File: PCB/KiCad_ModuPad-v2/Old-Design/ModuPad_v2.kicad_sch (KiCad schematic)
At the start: 95 parts, among them J1 Conn_01x02, J2 OLED_128x32, SW1 SW_Push, SW10 SW_Push, SW11 SW_Push, SW12 SW_Push, SW13 SW_Push, SW14 SW_Push, SW15 SW_Push, SW16 SW_Push, SW17 SW_Push, SW18 SW_Push, SW19 SW_Push, SW2 SW_Push, SW20 SW_Push, SW21 SW_Push, SW22 SW_Push, SW23 SW_Push, SW24 SW_Push, SW25 SW_Push, SW27_RST1 SW_Push_45deg, SW3 SW_Push, SW4 SW_Push, SW5 SW_Push, SW6 SW_Push, SW7 SW_Push, SW8 SW_Push, SW9 SW_Push

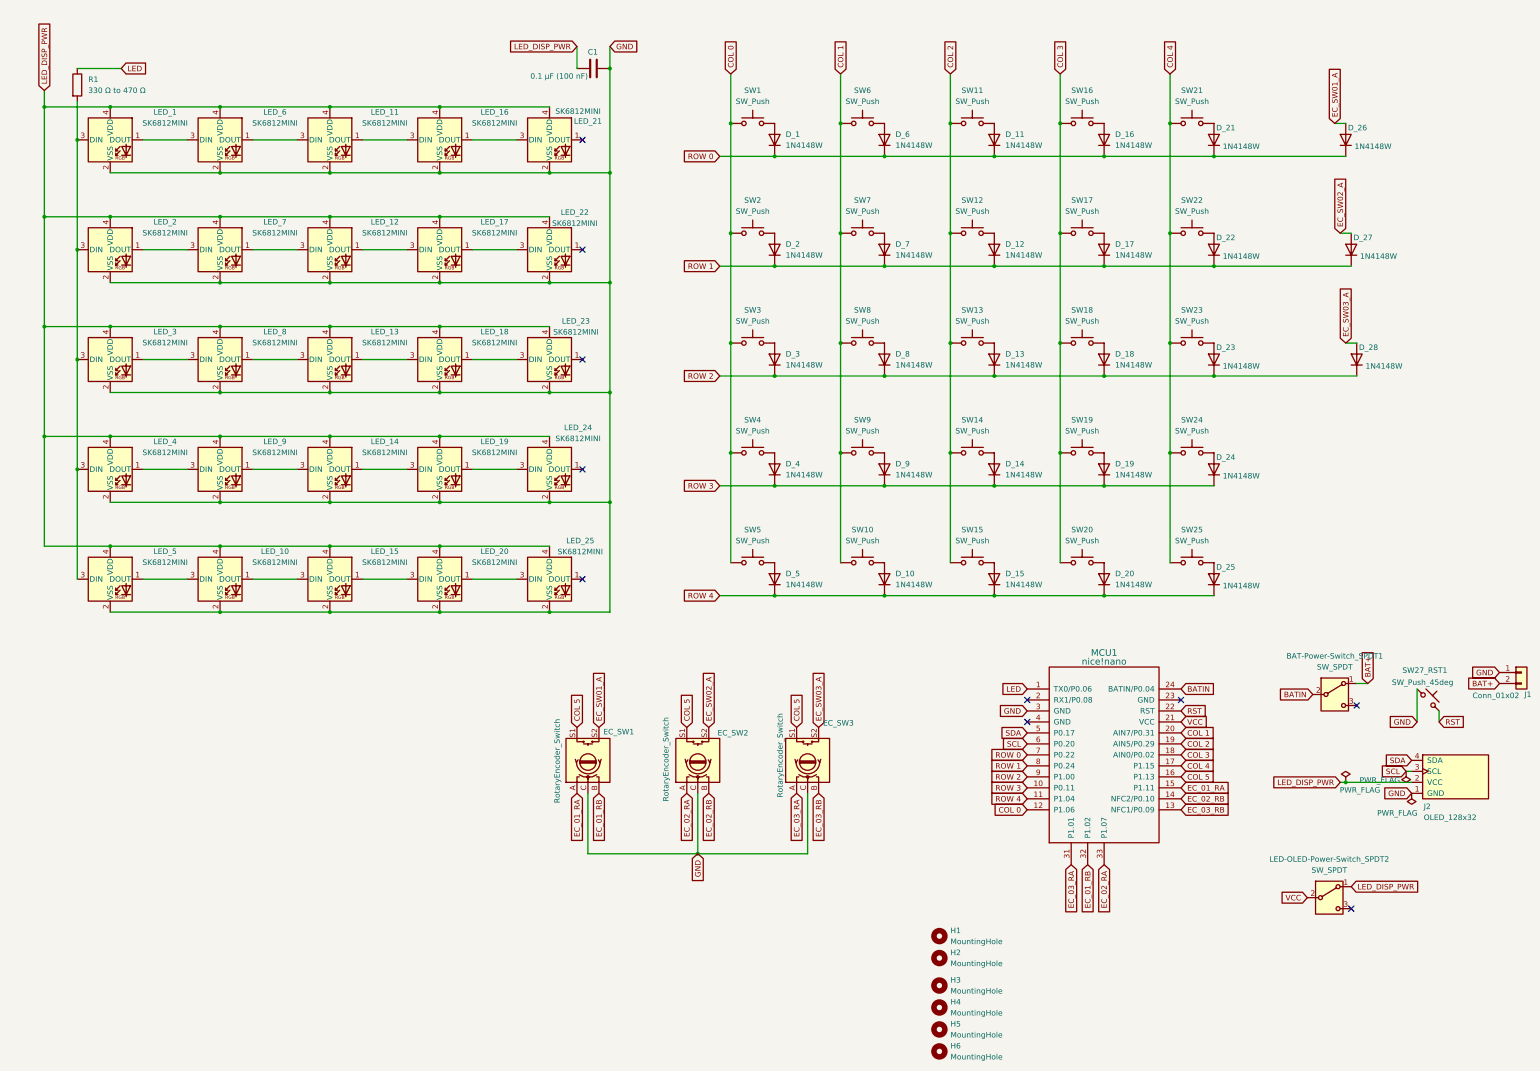
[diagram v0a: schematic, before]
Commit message: Update BOM and PCB
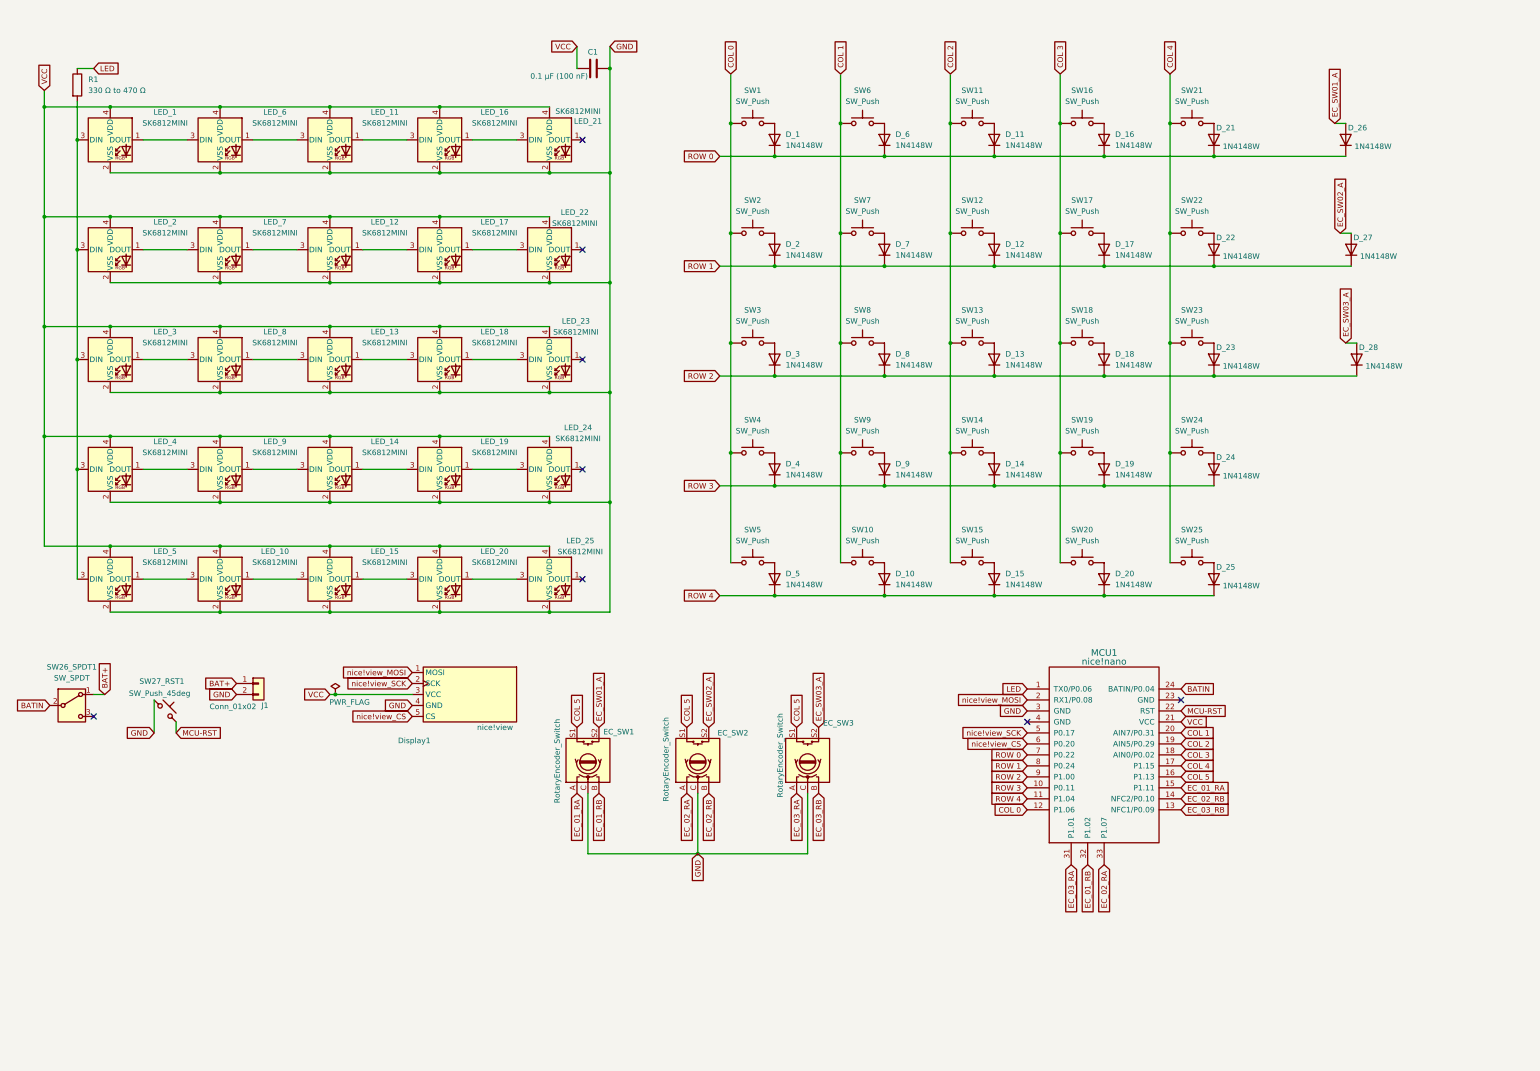
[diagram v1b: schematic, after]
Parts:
- removed H1, H2, H3, H4, H5, H6: MountingHole, MountingHole:MountingHole_2mm, symbol Mechanical:MountingHole
- removed J2: OLED_128x32, ScottoKeebs_Components:OLED_128x32, symbol ScottoKeebs:OLED_128x32
- removed LED-OLED-Power-Switch_SPDT2: SW_SPDT, Power-Switch-Battery:SPDT_C128955, symbol Switch:SW_SPDT
- added Display1: nice!view, nice!view:nice_view, symbol nice_view:nice!view
- C1: footprint Capacitor_THT:CP_Radial_D6.3mm_P2.50mm -> Capacitor_SMD:C_0603_1608Metric
- D_1, D_10, D_11, D_12, D_13, D_14, D_15, D_16, D_17, D_18, D_19, D_2, D_20, D_21, D_22, D_23, D_24, D_25, D_26, D_27, D_28, D_3, D_4, D_5, D_6, D_7, D_8, D_9: footprint ScottoKeebs_Components:Diode_SOD-123 -> Diode_SMD:D_SOD-123
- LED_1, LED_10, LED_11, LED_12, LED_13, LED_14, LED_15, LED_16, LED_17, LED_18, LED_19, LED_2, LED_20, LED_21, LED_22, LED_23, LED_24, LED_25, LED_3, LED_4, LED_5, LED_6, LED_7, LED_8, LED_9: footprint SK6812MINI-E:LED_SK6812MINI -> SK6812MINI-E:SK6812MINI-E
- R1: footprint Resistor_THT:R_Axial_DIN0207_L6.3mm_D2.5mm_P10.16mm_Horizontal -> Resistor_SMD:R_0603_1608Metric_Pad0.98x0.95mm_HandSolder
- SW1, SW10, SW11, SW12, SW13, SW14, SW15, SW16, SW17, SW18, SW19, SW2, SW20, SW21, SW22, SW23, SW24, SW25, SW3, SW4, SW5, SW6, SW7, SW8, SW9: footprint ScottoKeebs_Hotswap:Hotswap_MX_1.00u -> MX-Style-Cherry-Switches-with-Kilah-HotSwap-Socket:SW_MX_HS_CPG151101S11_1u
- renumbered BAT-Power-Switch_SPDT1 to SW26_SPDT1
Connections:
- net LED_DISP_PWR is gone; now on net VCC: C1.1, LED_1.4 (VDD), LED_10.4 (VDD), LED_11.4 (VDD), LED_12.4 (VDD), LED_13.4 (VDD), LED_14.4 (VDD), LED_15.4 (VDD), LED_16.4 (VDD), LED_17.4 (VDD), LED_18.4 (VDD), LED_19.4 (VDD), LED_2.4 (VDD), LED_20.4 (VDD), LED_21.4 (VDD), LED_22.4 (VDD), LED_23.4 (VDD), LED_24.4 (VDD), LED_25.4 (VDD), LED_3.4 (VDD), LED_4.4 (VDD), LED_5.4 (VDD), LED_6.4 (VDD), LED_7.4 (VDD), LED_8.4 (VDD), LED_9.4 (VDD)
- net BAT+: now also J1.1 (Pin_1); no longer J1.2 (Pin_2)
- net GND: now also J1.2 (Pin_2), Display1.4 (GND); no longer J1.1 (Pin_1)
- net VCC: now also Display1.3 (VCC)
- net nice!view_MOSI: now reaches MCU1.2 (RX1/P0.08)
- net nice!view_MOSI: now also Display1.1 (MOSI)
- net RST renamed MCU-RST
- net SCL renamed nice!view_CS
- net nice!view_CS: now also Display1.5 (CS)
- net SDA renamed nice!view_SCK
- net nice!view_SCK: now also Display1.2 (SCK)
- no-connect marks 10 -> 8
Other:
- moved on the sheet: J1, SW26_SPDT1, SW27_RST1
